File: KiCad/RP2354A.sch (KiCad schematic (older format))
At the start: 8 parts, among them J11 Conn_01x02, U16 RP2354A, Y1 ABM8-272-T3

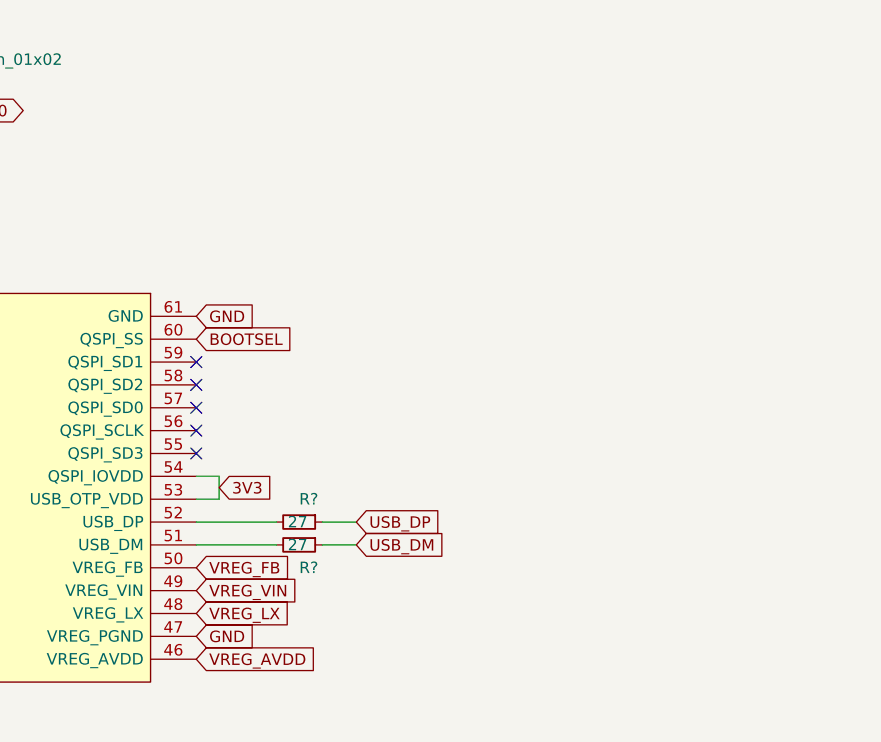
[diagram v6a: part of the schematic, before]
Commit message: Place USB-C connector for the RP2354A (U16) and route the USB_DP,USB_DM signals
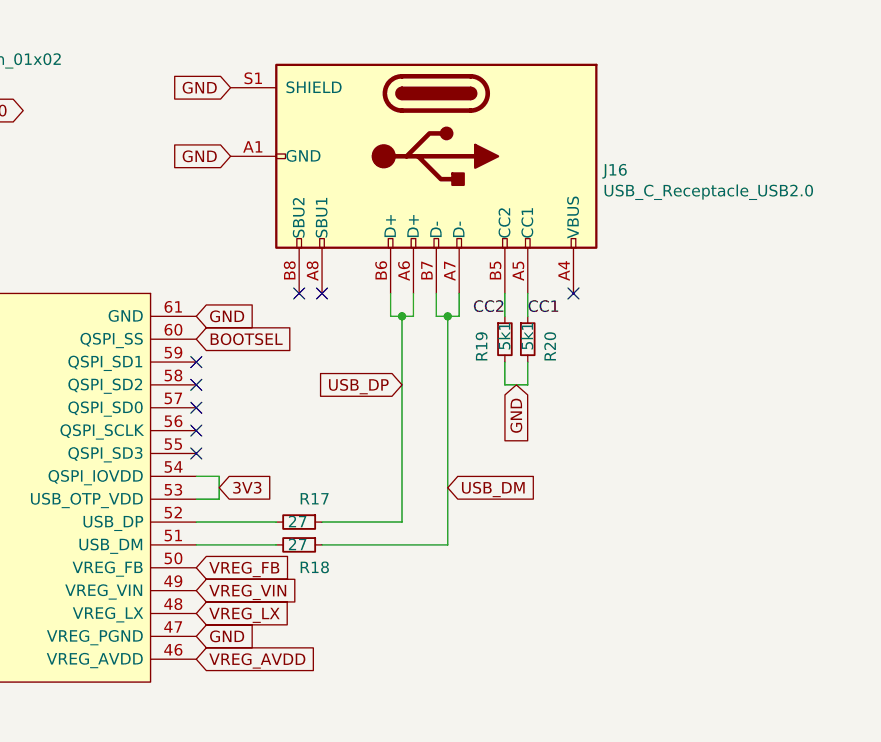
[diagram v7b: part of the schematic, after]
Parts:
- added J16: USB_C_Receptacle_USB2.0, Connector_USB:USB_C_Receptacle_HRO_TYPE-C-31-M-12, symbol Connector:USB_C_Receptacle_USB2.0
- added R19, R20: 5k1, Resistor_SMD:R_0603_1608Metric_Pad0.98x0.95mm_HandSolder, symbol Device:R_Small
- gave numbers to parts that had none: 2
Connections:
- net GND: now also J16.A1 (GND), J16.A12 (GND), J16.B1 (GND), J16.B12 (GND), J16.S1 (SHIELD), R19.2, R20.2
- net USB_DM: now also J16.A7 (D-), J16.B7 (D-)
- net USB_DP: now also J16.A6 (D+), J16.B6 (D+)
- new net: J16.A4 (VBUS), J16.A9 (VBUS), J16.B4 (VBUS), J16.B9 (VBUS)
- new net CC1: J16.A5 (CC1), R20.1
- new net CC2: J16.B5 (CC2), R19.1
- no-connect marks 23 -> 26
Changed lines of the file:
@@
 Text GLabel 6900 2700 2    50   Input ~ 0
 GND
-Text GLabel 7600 3600 2    50   Input ~ 0
+Text GLabel 7800 3000 0    50   Input ~ 0
 USB_DP
-Text GLabel 7600 3700 2    50   Input ~ 0
+Text GLabel 8000 3450 2    50   Input ~ 0
 USB_DM
 Text GLabel 5900 2400 1    50   Input ~ 0
@@
 P 7350 3600
 AR Path="/6ADC9F07" Ref="R?"  Part="1"
-AR Path="/6AFE5B10/6ADC9F07" Ref="R?"  Part="1"
-F 0 "R?" V 7250 3600 50  0000 L CNN
+AR Path="/6AFE5B10/6ADC9F07" Ref="R17"  Part="1"
+F 0 "R17" V 7250 3600 50  0000 L CNN
 F 1 "27" V 7350 3550 50  0000 L CNN
 F 2 "Resistor_SMD:R_0603_1608Metric_Pad0.98x0.95mm_HandSolder" H 7350 3600 50  0001 C CNN
@@
 Wire Wire Line
 	6900 3600 7250 3600
-Wire Wire Line
-	7450 3600 7600 3600
 $Comp
 L Device:R_Small R?
@@
 P 7350 3700
 AR Path="/6ADD8B0E" Ref="R?"  Part="1"
-AR Path="/6AFE5B10/6ADD8B0E" Ref="R?"  Part="1"
-F 0 "R?" V 7450 3700 50  0000 L CNN
+AR Path="/6AFE5B10/6ADD8B0E" Ref="R18"  Part="1"
+F 0 "R18" V 7450 3700 50  0000 L CNN
 F 1 "27" V 7350 3650 50  0000 L CNN
 F 2 "Resistor_SMD:R_0603_1608Metric_Pad0.98x0.95mm_HandSolder" H 7350 3700 50  0001 C CNN
@@
 Wire Wire Line
 	6900 3700 7250 3700
-Wire Wire Line
-	7450 3700 7600 3700
+$Comp
+L Connector:USB_C_Receptacle_USB2.0 J16
+U 1 1 6AE0E79A
+P 7950 2000
+F 0 "J16" V 8011 2730 50  0000 L CNN
+F 1 "USB_C_Receptacle_USB2.0" V 8102 2730 50  0000 L CNN
+F 2 "Connector_USB:USB_C_Receptacle_HRO_TYPE-C-31-M-12" H 8100 2000 50  0001 C CNN
+F 3 "https://www.usb.org/sites/default/files/documents/usb_type-c.zip" H 8100 2000 50  0001 C CNN
+	1    7950 2000
+	0    1    1    0
+$EndComp
+Wire Wire Line
+	7750 2600 7750 2700
+Wire Wire Line
+	7850 2600 7850 2700
+Wire Wire Line
+	7750 2700 7800 2700
+Wire Wire Line
+	7950 2600 7950 2700
+Wire Wire Line
+	8050 2600 8050 2700
+Wire Wire Line
+	7950 2700 8000 2700
+Text GLabel 7050 2000 0    50   Input ~ 0
+GND
+Text GLabel 7050 1700 0    50   Input ~ 0
+GND
+$Comp
+L Device:R_Small R19
+U 1 1 6AE0E7AA
+P 8250 2800
+F 0 "R19" V 8150 2700 50  0000 L CNN
+F 1 "5k1" V 8250 2750 50  0000 L CNN
+F 2 "Resistor_SMD:R_0603_1608Metric_Pad0.98x0.95mm_HandSolder" H 8250 2800 50  0001 C CNN
+F 3 "~" H 8250 2800 50  0001 C CNN
+	1    8250 2800
+	1    0    0    -1
+$EndComp
+Wire Wire Line
+	8250 2600 8250 2700
+Text Label 8250 2700 2    50   ~ 0
+CC2
+Text GLabel 8300 3000 3    50   Input ~ 0
+GND
+$Comp
+L Device:R_Small R20
+U 1 1 6AE0E7B3
+P 8350 2800
+F 0 "R20" V 8450 2700 50  0000 L CNN
+F 1 "5k1" V 8350 2750 50  0000 L CNN
+F 2 "Resistor_SMD:R_0603_1608Metric_Pad0.98x0.95mm_HandSolder" H 8350 2800 50  0001 C CNN
+F 3 "~" H 8350 2800 50  0001 C CNN
+	1    8350 2800
+	1    0    0    -1
+$EndComp
+Wire Wire Line
+	8350 2600 8350 2700
+Text Label 8350 2700 0    50   ~ 0
+CC1
+Wire Wire Line
+	8250 2900 8250 3000
+Wire Wire Line
+	8350 2900 8350 3000
+Wire Wire Line
+	8250 3000 8350 3000
+NoConn ~ 7350 2600
+NoConn ~ 7450 2600
+NoConn ~ 8550 2600
+Wire Wire Line
+	7800 2700 7800 3600
+Wire Wire Line
+	7450 3600 7800 3600
+Connection ~ 7800 2700
+Wire Wire Line
+	7800 2700 7850 2700
+Wire Wire Line
+	8000 2700 8000 3700
+Wire Wire Line
+	7450 3700 8000 3700
+Connection ~ 8000 2700
+Wire Wire Line
+	8000 2700 8050 2700
 $EndSCHEMATC

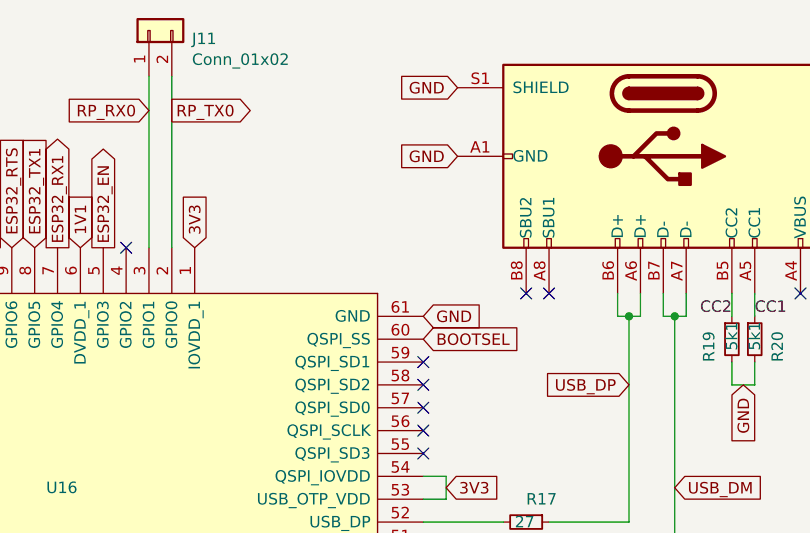
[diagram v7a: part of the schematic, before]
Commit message: Add a push-button for BOOTSEL signal
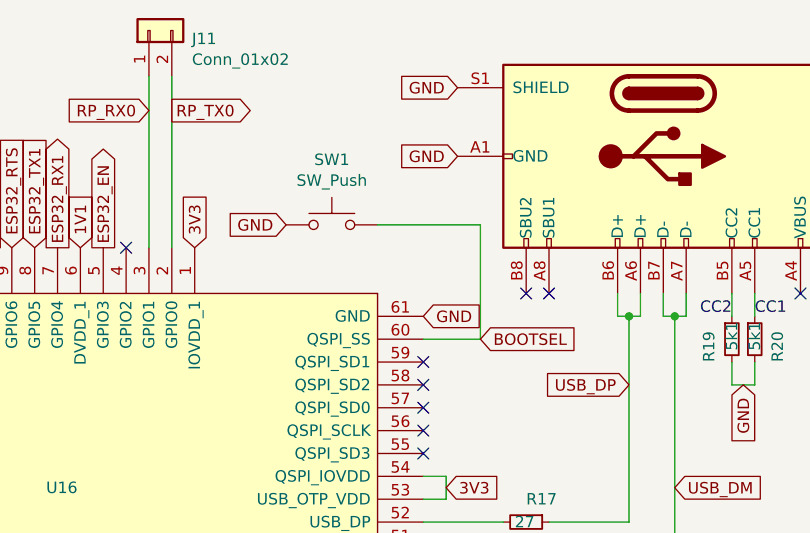
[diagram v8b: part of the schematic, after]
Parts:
- added SW1: SW_Push, SF2000:Sunrom_Tactile_Switch_3x4x2mm_SMD_2-Pin, symbol Switch:SW_Push
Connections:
- net BOOTSEL: now also SW1.2
- net GND: now also SW1.1
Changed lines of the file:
@@
 Wire Wire Line
 	5800 1650 5800 2400
-Text GLabel 6900 2800 2    50   Input ~ 0
+Text GLabel 7150 2800 2    50   Input ~ 0
 BOOTSEL
 $Comp
@@
 Wire Wire Line
 	8000 2700 8050 2700
+$Comp
+L Switch:SW_Push SW1
+U 1 1 6AE2E6BB
+P 6500 2300
+F 0 "SW1" H 6500 2585 50  0000 C CNN
+F 1 "SW_Push" H 6500 2494 50  0000 C CNN
+F 2 "SF2000:Sunrom_Tactile_Switch_3x4x2mm_SMD_2-Pin" H 6500 2500 50  0001 C CNN
+F 3 "~" H 6500 2500 50  0001 C CNN
+	1    6500 2300
+	1    0    0    -1
+$EndComp
+Wire Wire Line
+	6900 2800 7150 2800
+Wire Wire Line
+	7150 2800 7150 2300
+Wire Wire Line
+	7150 2300 6700 2300
+Text GLabel 6300 2300 0    50   Input ~ 0
+GND
 $EndSCHEMATC
